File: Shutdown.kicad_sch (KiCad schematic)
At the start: 43 parts, among them J1 0194270049, Q1 SI2347DS-T1-GE3, Q2 SI2347DS-T1-GE3, Q4 SI2318CDS-T1-GE3, Q5 SI2318CDS-T1-GE3, Q6 SI2318CDS-T1-GE3, Q7 SI2347DS-T1-GE3

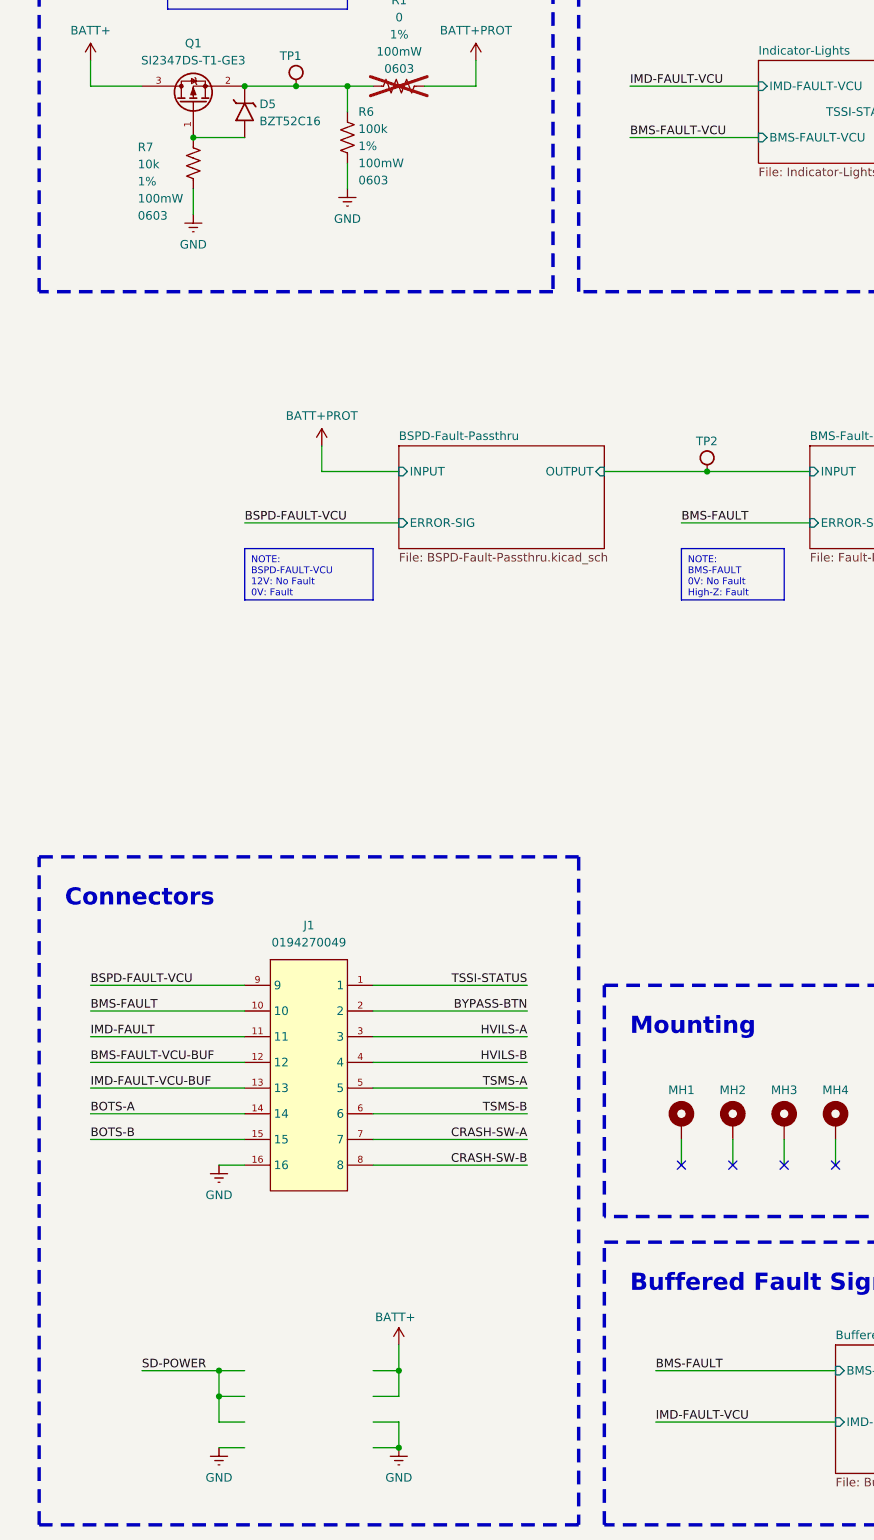
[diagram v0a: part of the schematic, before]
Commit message: added in second connector for power, SD power, debug
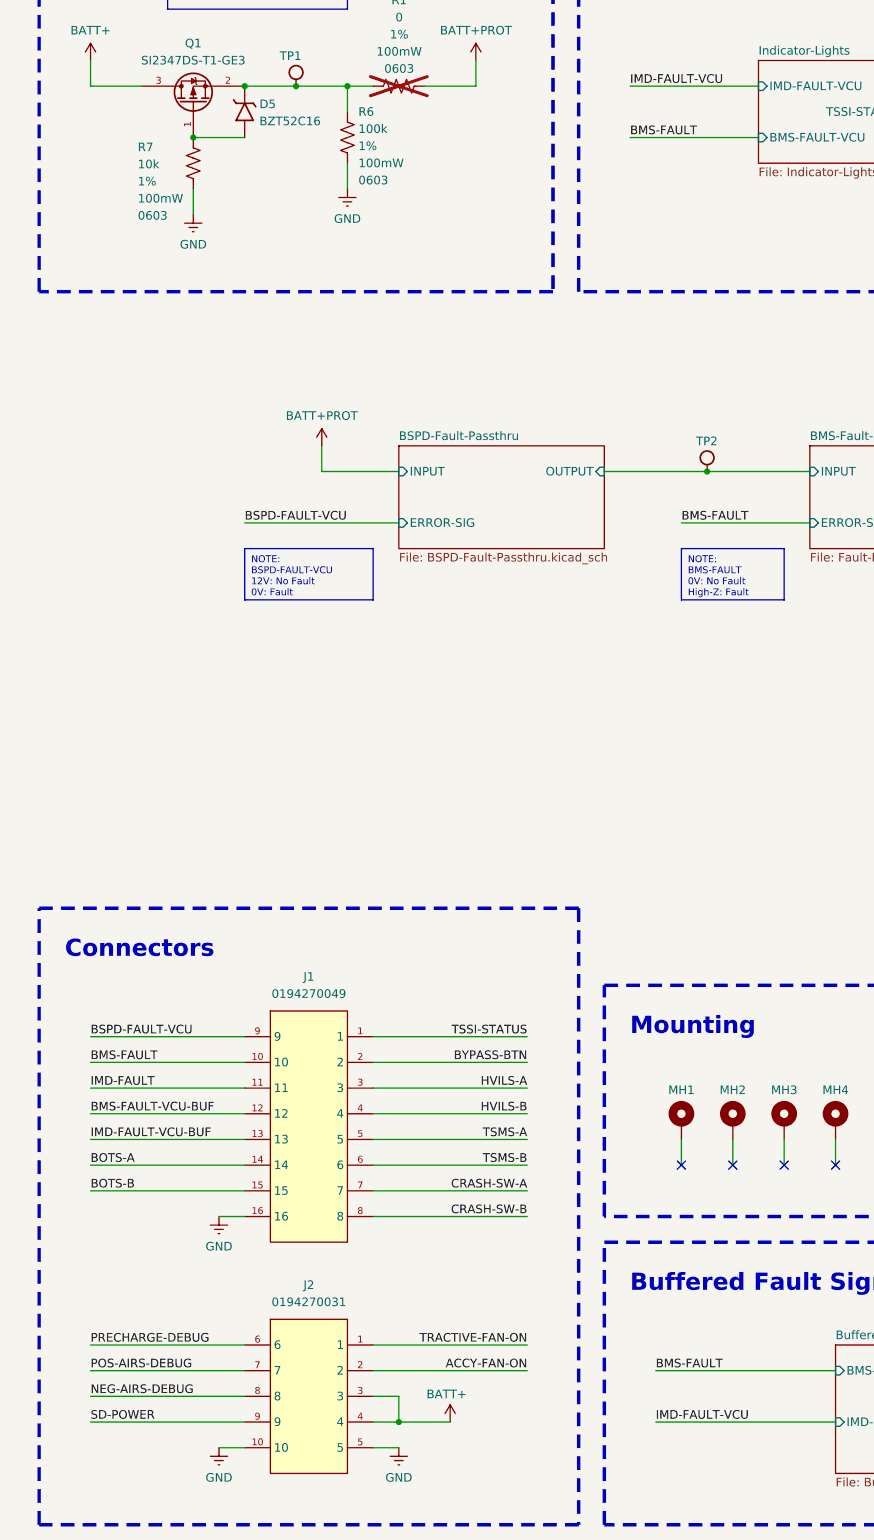
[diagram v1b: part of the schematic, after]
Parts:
- added J2: 0194270031, -Connectors:0194270049, symbol -Connectors:0194270031
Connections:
- net BATT+: now also J2.3, J2.4
- net GND: now also J2.10, J2.5
- net SD-POWER: now also J2.9
- new net ACCY-FAN-ON: J2.2
- new net NEG-AIRS-DEBUG: J2.8
- new net POS-AIRS-DEBUG: J2.7
- new net PRECHARGE-DEBUG: J2.6
- new net TRACTIVE-FAN-ON: J2.1
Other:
- moved on the sheet: J1

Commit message: cleaning port names
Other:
- sheet Buffered-Faults ports: added BMS-FAULT; removed BMS-FAULT-VCU
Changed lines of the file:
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@@
-			)
-		)
-		(pin "BMS-FAULT-VCU" input
-			(at 137.16 255.27 180)
-			(effects
-				(font
-					(size 1.27 1.27)
-				)
-				(justify left)
 			)
 		)
@@
 			)
 		)
+		(pin "BMS-FAULT" input
+			(at 137.16 255.27 180)
+			(effects
+				(font
+					(size 1.27 1.27)
+				)
+				(justify left)
+			)
+		)

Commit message: updating component properties
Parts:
- J2: footprint -Connectors:0194270049 -> -Connectors:0194270031; Digikey P/N (none) -> 23-0194270031-ND; LCSC P/N (none) -> C17317250; Link (none) -> https://www.digikey.com/en/products/detail/molex/0194270031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; Manufacturer P/N (none) -> 0194270031; Mouser P/N (none) -> 538-19427-0031
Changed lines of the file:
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@@
 			)
 		)
-		(property "Footprint" "-Connectors:0194270049"
+		(property "Footprint" "-Connectors:0194270031"
 			(at 53.34 281.94 0)
 			(effects
@@
 			)
 		)
-		(property "Datasheet" ""
+		(property "Datasheet" "https://www.molex.com/content/dam/molex/molex-dot-com/products/automated/en-us/salesdrawingpdf/194/19427/194270031_sd.pdf?inline"
 			(at 53.34 285.75 0)
 			(effects
@@
 			)
 		)
-		(property "Description" ""
+		(property "Description" "Connector Header Panel Mount, Through Hole, Right Angle 10 position 0.230\" (5.84mm)"
 			(at 53.34 289.56 0)
 			(effects
@@
 			)
 		)
-		(property "Link" ""
+		(property "Link" "https://www.digikey.com/en/products/detail/molex/0194270031/863312?s=N4IgTCBcDaIIwE4AsYDsAGdBmOIC6AvkA"
 			(at 53.34 293.37 0)
 			(effects
@@
 			)
 		)
-		(property "Manufacturer P/N" ""
+		(property "Manufacturer P/N" "0194270031"
 			(at 53.34 300.99 0)
 			(effects
@@
 			)
 		)
-		(property "Digikey P/N" ""
+		(property "Digikey P/N" "23-0194270031-ND"
 			(at 53.34 304.8 0)
 			(effects
@@
 			)
 		)
-		(property "Mouser P/N" ""
+		(property "Mouser P/N" "538-19427-0031"
 			(at 53.34 308.61 0)
 			(effects
@@
 			)
 		)
-		(property "LCSC P/N" ""
+		(property "LCSC P/N" "C17317250"
 			(at 53.34 312.42 0)
 			(effects

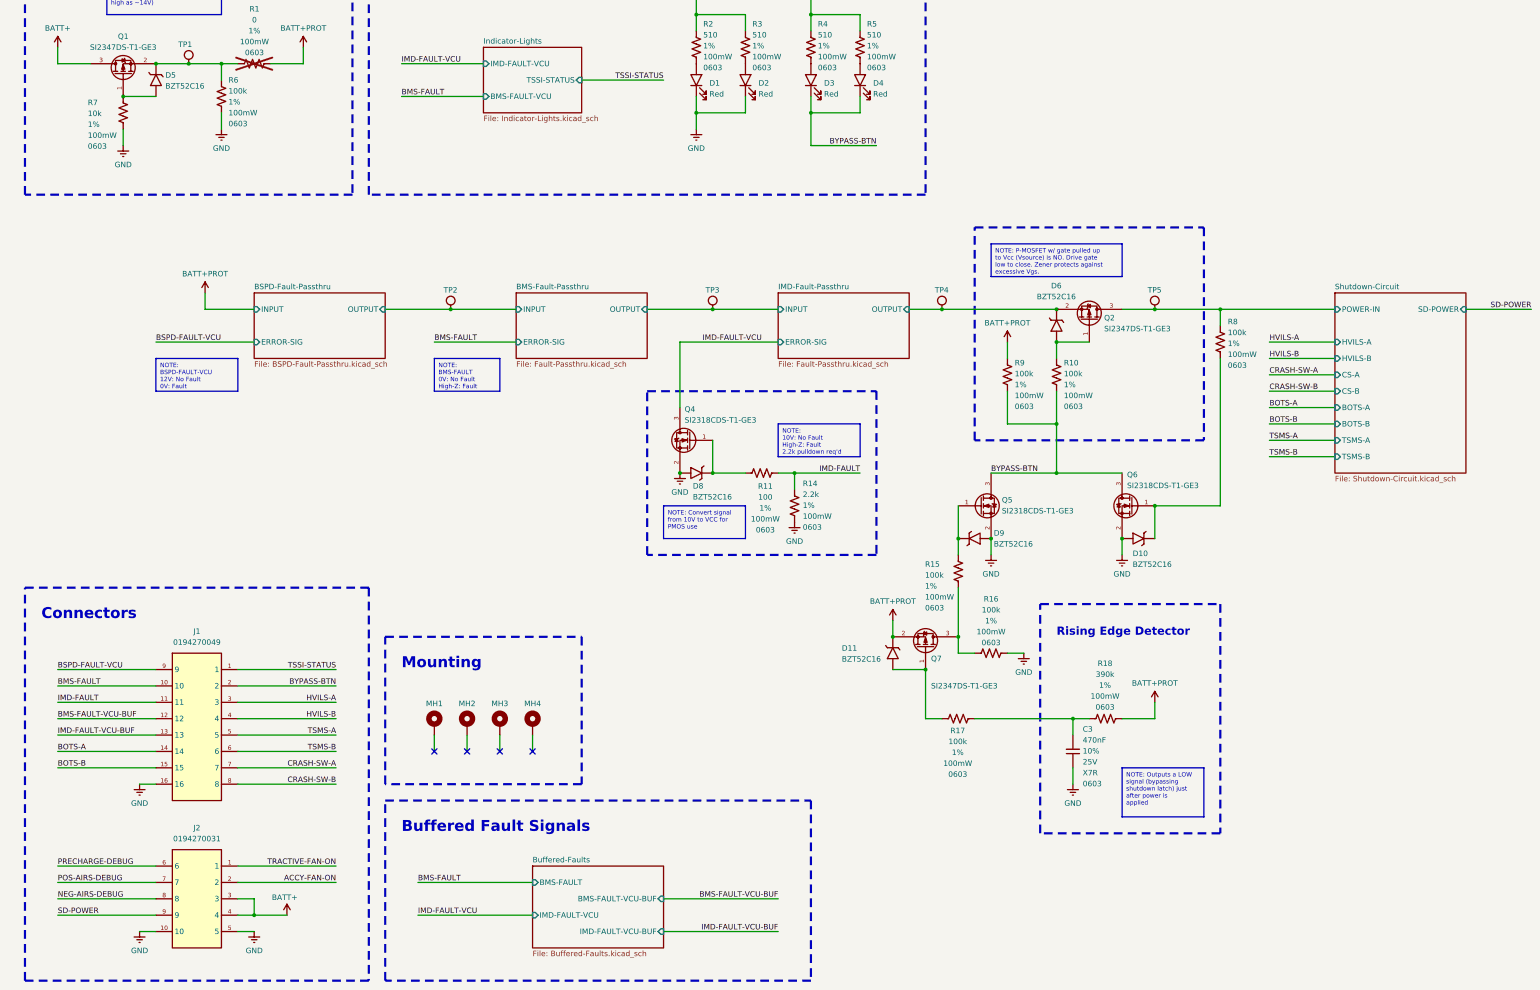
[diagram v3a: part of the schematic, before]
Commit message: updated port directionalities, updated pinout
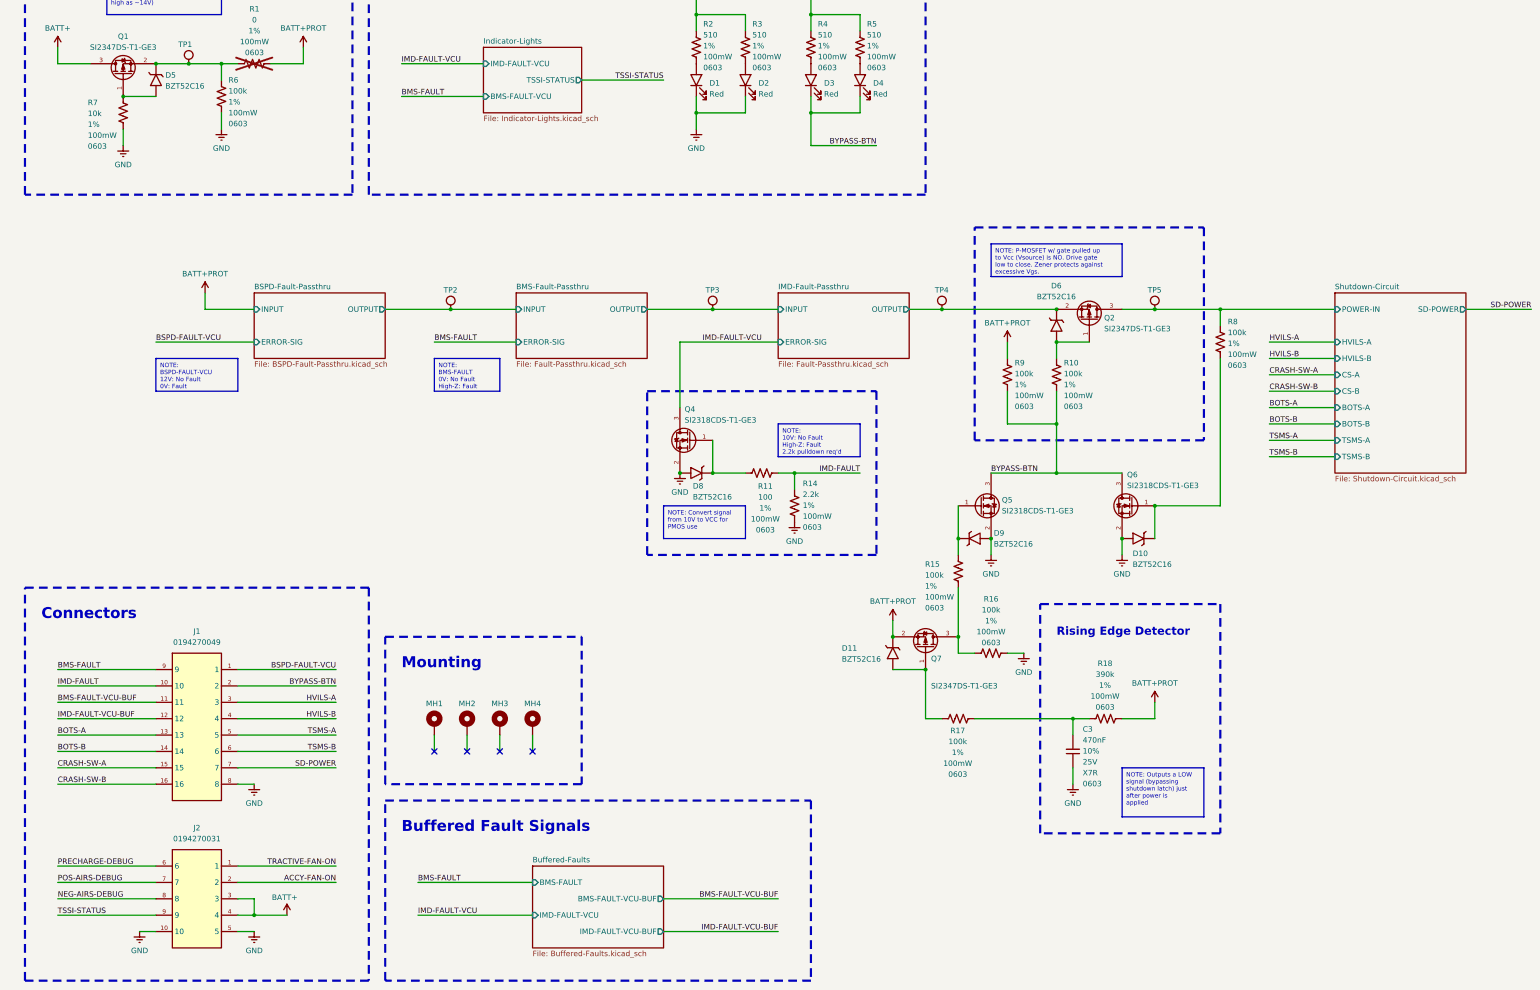
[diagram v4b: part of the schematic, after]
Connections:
- net BMS-FAULT: now also J1.9; no longer J1.10
- net BMS-FAULT-VCU-BUF: now also J1.11; no longer J1.12
- net BOTS-A: now also J1.13; no longer J1.14
- net BOTS-B: now also J1.14; no longer J1.15
- net BSPD-FAULT-VCU: now also J1.1; no longer J1.9
- net CRASH-SW-A: now also J1.15; no longer J1.7
- net CRASH-SW-B: now also J1.16; no longer J1.8
- net GND: now also J1.8; no longer J1.16
- net IMD-FAULT: now also J1.10; no longer J1.11
- net IMD-FAULT-VCU-BUF: now also J1.12; no longer J1.13
- net SD-POWER: now also J1.7; no longer J2.9
- net TSSI-STATUS: now also J2.9; no longer J1.1
